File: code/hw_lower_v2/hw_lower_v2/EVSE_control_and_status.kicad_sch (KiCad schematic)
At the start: 13 parts, among them U3 DRV8220DRL, U4 TLV1805

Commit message: further lower board sch work
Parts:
- added C12, C13: 22uF 25V, Capacitor_SMD:C_1210_3225Metric, symbol Device:C
- C4: value C -> 100n; footprint (none) -> Capacitor_SMD:C_0805_2012Metric
- C5, C6: value C -> 100n 25V; footprint (none) -> Capacitor_SMD:C_0805_2012Metric
- R18, R19, R20, R21: footprint (none) -> Resistor_SMD:R_0603_1608Metric
- R22: value 1K -> 200k; footprint (none) -> Resistor_SMD:R_0603_1608Metric
- R23: value 1K -> 66.5k; footprint (none) -> Resistor_SMD:R_0603_1608Metric
- R24: value 1K -> 56k; footprint (none) -> Resistor_SMD:R_0603_1608Metric
- U3: footprint (none) -> Package_TO_SOT_SMD:SOT-563
- U4: footprint (none) -> Package_TO_SOT_SMD:SOT-23
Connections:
- net +12V: now also C12.1, C13.1
- net GND: now also C12.2, C13.2
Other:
- moved on the sheet: C4, C5, D2, R19, R20, R21, R22, R23, R24, U4

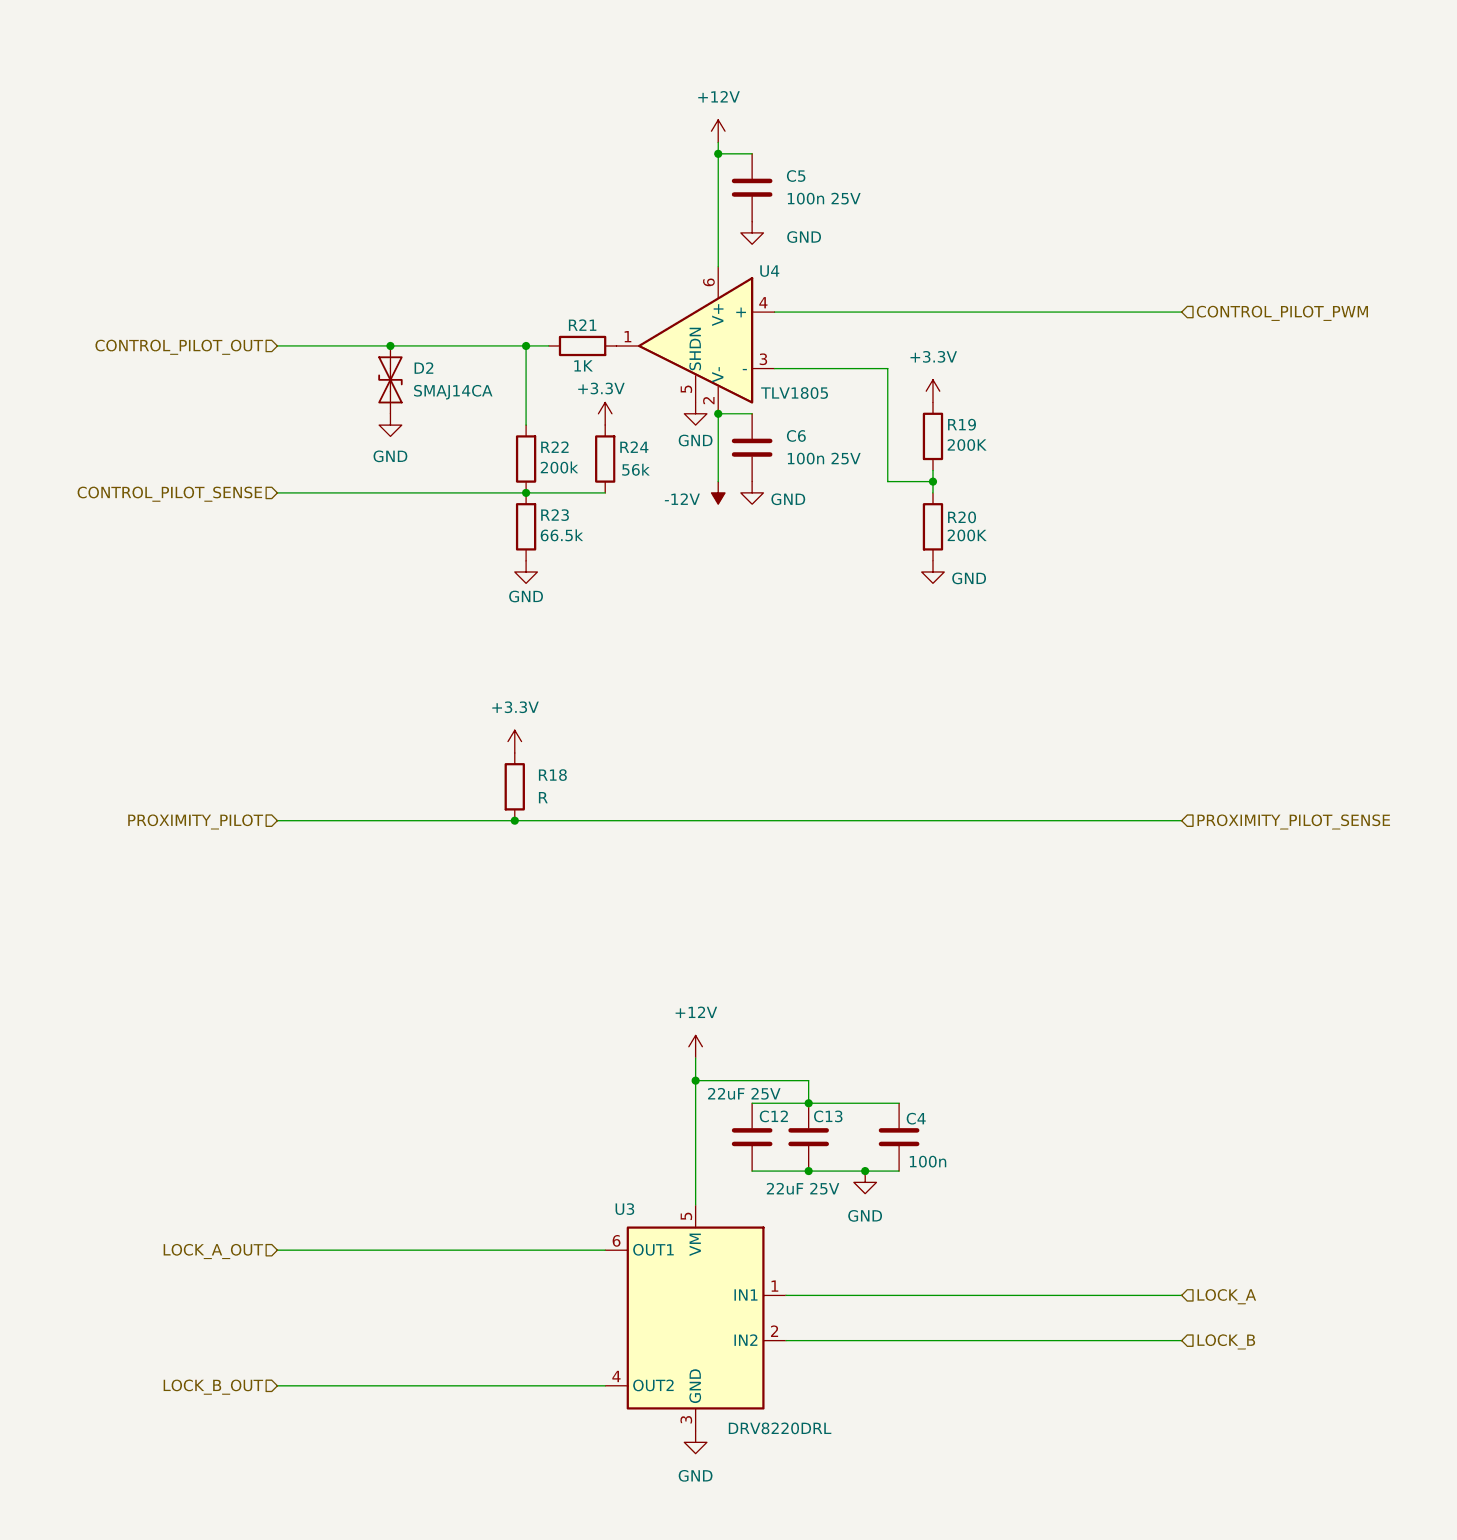
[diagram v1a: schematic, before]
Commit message: add 12V voltage inverter and polish
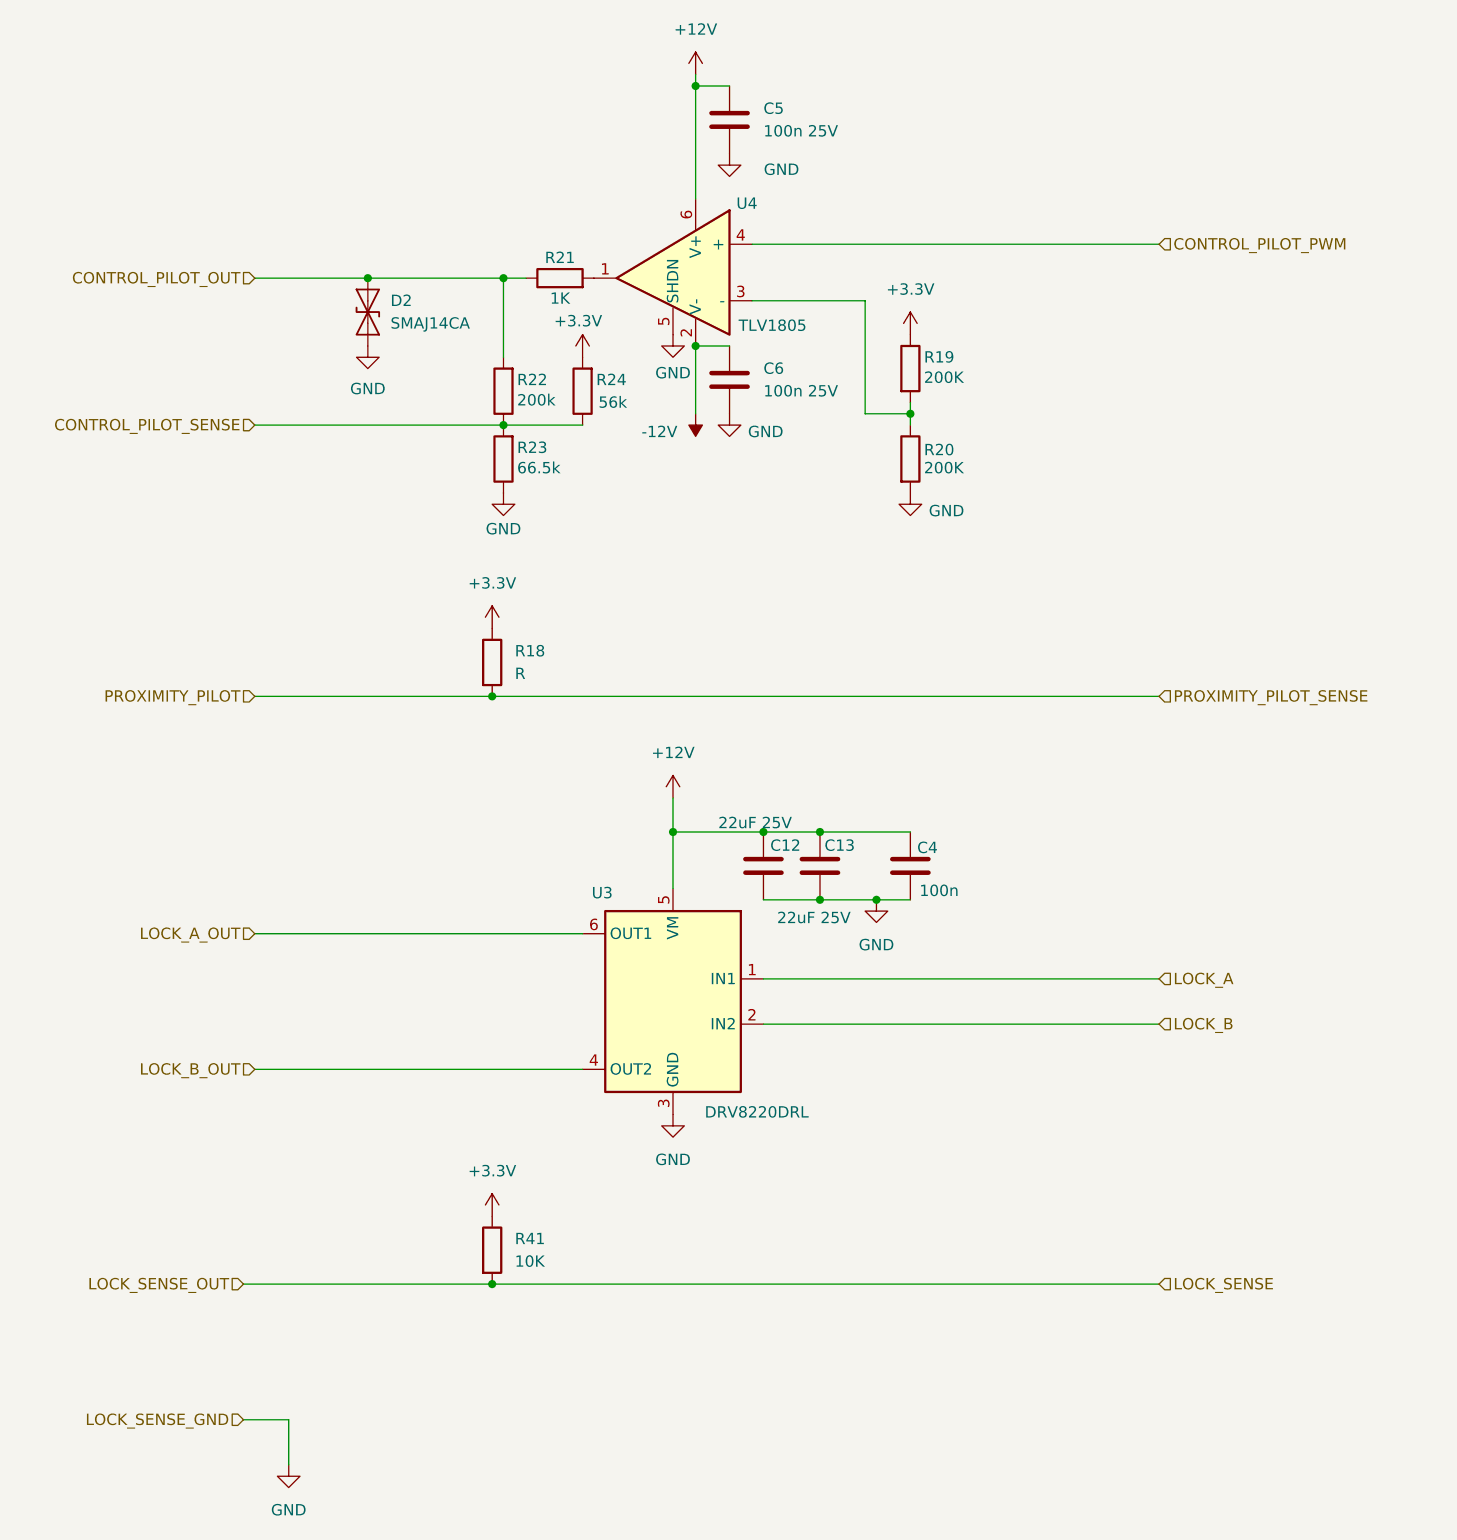
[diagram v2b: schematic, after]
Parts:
- added R41: 10K, Resistor_SMD:R_0603_1608Metric, symbol Device:R
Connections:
- net +3.3V: now also R41.1
- new net LOCK_SENSE: R41.2
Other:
- moved on the sheet: C12, C13, C4, C5, C6, D2, R18, R19, R20, R21, R22, R23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

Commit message: schematic is done
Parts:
- removed C12, C13: 22uF 25V, Capacitor_SMD:C_1210_3225Metric, symbol Device:C
- added C23: 10u, symbol Device:C_Polarized
- added D6: SMAJ5.0A, Diode_SMD:D_SMA, symbol Diode:SMAJ5.0A
- C5, C6: value 100n 25V -> 100n
- D2: JLCPCB Part # (none) -> C908820
- R18: value R -> 1K
- R22: value 200k -> 200k 1%
- R23: value 66.5k -> 66.5k 1%
- U3: JLCPCB Part # (none) -> C3681351
- U4: JLCPCB Part # (none) -> C2862164
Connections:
- net +12V: now also C23.1
- net GND: now also C23.2, D6.2 (A2)
- net LOCK_SENSE: now also D6.1 (A1)
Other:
- note added: "PP resistance 100ohm 10 mm2 62A 220ohm 6 mm2 32A 680ohm 2.5mm2 20A 1500ohm 1.5mm2 10A"
- moved on the sheet: C4, R24

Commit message: finishing up sch and creating footprints
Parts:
- renumbered C23 to C10, C4 to C11, C5 to C8, C6 to C9, D6 to D2, D2 to D3, R18 to R29, R41 to R30, R22 to R31, R23 to R32, R21 to R33, R24 to R34, R19 to R35, R20 to R36
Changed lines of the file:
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@@
 		(on_board yes)
 		(dnp no)
-		(property "Reference" "#PWR024"
+		(property "Reference" "#PWR047"
 			(at 101.6 35.56 0)
 			(effects
@@
 			(project "hw_lower_v2"
 				(path "/c5175f1c-553a-46da-abbd-483c59ad8dfa/8ba574d6-efbf-49a1-9fad-b0d96c57b1a3"
-					(reference "#PWR024")
+					(reference "#PWR047")
 					(unit 1)
 				)
@@
 		(on_board yes)
 		(dnp no)
-		(property "Reference" "#PWR028"
+		(property "Reference" "#PWR051"
 			(at 121.92 73.66 0)
 			(effects
@@
 			(project "hw_lower_v2"
 				(path "/c5175f1c-553a-46da-abbd-483c59ad8dfa/8ba574d6-efbf-49a1-9fad-b0d96c57b1a3"
-					(reference "#PWR028")
+					(reference "#PWR051")
 					(unit 1)
 				)
@@
 		(dnp no)
 		(fields_autoplaced yes)
-		(property "Reference" "#PWR020"
+		(property "Reference" "#PWR043"
 			(at 95.25 105.41 0)
 			(effects
@@
 			(project ""
 				(path "/c5175f1c-553a-46da-abbd-483c59ad8dfa/8ba574d6-efbf-49a1-9fad-b0d96c57b1a3"
-					(reference "#PWR020")
+					(reference "#PWR043")
 					(unit 1)
 				)
@@
 		(dnp no)
 		(fields_autoplaced yes)
-		(property "Reference" "R41"
+		(property "Reference" "R30"
 			(at 77.47 151.1299 0)
 			(effects
@@
 			(project "hw_lower_v2"
 				(path "/c5175f1c-553a-46da-abbd-483c59ad8dfa/8ba574d6-efbf-49a1-9fad-b0d96c57b1a3"
-					(reference "R41")
+					(reference "R30")
 					(unit 1)
 				)
@@
 		(dnp no)
 		(fields_autoplaced yes)
-		(property "Reference" "#PWR050"
+		(property "Reference" "#PWR049"
 			(at 110.49 119.38 0)
 			(effects
@@
 			(project "hw_lower_v2"
 				(path "/c5175f1c-553a-46da-abbd-483c59ad8dfa/8ba574d6-efbf-49a1-9fad-b0d96c57b1a3"
-					(reference "#PWR050")
+					(reference "#PWR049")
 					(unit 1)
 				)
@@
 		(on_board yes)
 		(dnp no)
-		(property "Reference" "R24"
+		(property "Reference" "R34"
 			(at 89.154 54.61 0)
 			(effects
@@
 			(project "hw_lower_v2"
 				(path "/c5175f1c-553a-46da-abbd-483c59ad8dfa/8ba574d6-efbf-49a1-9fad-b0d96c57b1a3"
-					(reference "R24")
+					(reference "R34")
 					(unit 1)
 				)
@@
 		(on_board yes)
 		(dnp no)
-		(property "Reference" "#PWR026"
+		(property "Reference" "#PWR046"
 			(at 97.79 54.61 0)
 			(effects
@@
 			(project ""
 				(path "/c5175f1c-553a-46da-abbd-483c59ad8dfa/8ba574d6-efbf-49a1-9fad-b0d96c57b1a3"
-					(reference "#PWR026")
+					(reference "#PWR046")
 					(unit 1)
 				)
@@
 		(on_board yes)
 		(dnp no)
-		(property "Reference" "R21"
+		(property "Reference" "R33"
 			(at 82.55 40.894 90)
 			(effects
@@
 			(project "hw_lower_v2"
 				(path "/c5175f1c-553a-46da-abbd-483c59ad8dfa/8ba574d6-efbf-49a1-9fad-b0d96c57b1a3"
-					(reference "R21")
+					(reference "R33")
 					(unit 1)
 				)
@@
 		(dnp no)
 		(fields_autoplaced yes)
-		(property "Reference" "D2"
+		(property "Reference" "D3"
 			(at 63.5 45.7199 90)
 			(effects
@@
 			(project ""
 				(path "/c5175f1c-553a-46da-abbd-483c59ad8dfa/8ba574d6-efbf-49a1-9fad-b0d96c57b1a3"
-					(reference "D2")
+					(reference "D3")
 					(unit 1)
 				)
@@
 		(dnp no)
 		(fields_autoplaced yes)
-		(property "Reference" "#PWR027"
+		(property "Reference" "#PWR050"
 			(at 121.92 53.34 0)
 			(effects
@@
 			(project "hw_lower_v2"
 				(path "/c5175f1c-553a-46da-abbd-483c59ad8dfa/8ba574d6-efbf-49a1-9fad-b0d96c57b1a3"
-					(reference "#PWR027")
+					(reference "#PWR050")
 					(unit 1)
 				)
@@
 		(on_board yes)
 		(dnp no)
-		(property "Reference" "#PWR034"
+		(property "Reference" "#PWR042"
 			(at 95.25 55.88 0)
 			(effects
@@
 			(project "hw_lower_v2"
 				(path "/c5175f1c-553a-46da-abbd-483c59ad8dfa/8ba574d6-efbf-49a1-9fad-b0d96c57b1a3"
-					(reference "#PWR034")
+					(reference "#PWR042")
 					(unit 1)
 				)
@@
 		(on_board yes)
 		(dnp no)
-		(property "Reference" "#PWR029"
+		(property "Reference" "#PWR040"
 			(at 76.2 73.66 0)
 			(effects
@@
 			(project "hw_lower_v2"
 				(path "/c5175f1c-553a-46da-abbd-483c59ad8dfa/8ba574d6-efbf-49a1-9fad-b0d96c57b1a3"
-					(reference "#PWR029")
+					(reference "#PWR040")
 					(unit 1)
 				)
@@
 		(on_board yes)
 		(dnp no)
-		(property "Reference" "#PWR023"
+		(property "Reference" "#PWR048"
 			(at 101.6 64.77 0)
 			(effects
@@
 			(project "hw_lower_v2"
 				(path "/c5175f1c-553a-46da-abbd-483c59ad8dfa/8ba574d6-efbf-49a1-9fad-b0d96c57b1a3"
-					(reference "#PWR023")
+					(reference "#PWR048")
 					(unit 1)
 				)
@@
 		(on_board yes)
 		(dnp no)
-		(property "Reference" "C23"
+		(property "Reference" "C10"
 			(at 105.664 106.68 0)
 			(effects
@@
 			(project "hw_lower_v2"
 				(path "/c5175f1c-553a-46da-abbd-483c59ad8dfa/8ba574d6-efbf-49a1-9fad-b0d96c57b1a3"
-					(reference "C23")
+					(reference "C10")
 					(unit 1)
 				)
@@
 		(dnp no)
 		(fields_autoplaced yes)
-		(property "Reference" "#PWR057"
+		(property "Reference" "#PWR039"
 			(at 74.93 152.4 0)
 			(effects
@@
 			(project "hw_lower_v2"
 				(path "/c5175f1c-553a-46da-abbd-483c59ad8dfa/8ba574d6-efbf-49a1-9fad-b0d96c57b1a3"
-					(reference "#PWR057")
+					(reference "#PWR039")
 					(unit 1)
 				)
@@
 		(dnp no)
 		(fields_autoplaced yes)
-		(property "Reference" "#PWR025"
+		(property "Reference" "#PWR045"
 			(at 97.79 24.13 0)
 			(effects
@@
 			(project ""
 				(path "/c5175f1c-553a-46da-abbd-483c59ad8dfa/8ba574d6-efbf-49a1-9fad-b0d96c57b1a3"
-					(reference "#PWR025")
+					(reference "#PWR045")
 					(unit 1)
 				)
@@
 		(dnp no)
 		(fields_autoplaced yes)
-		(property "Reference" "#PWR021"
+		(property "Reference" "#PWR044"
 			(at 95.25 143.51 0)
 			(effects
@@
 			(project ""
 				(path "/c5175f1c-553a-46da-abbd-483c59ad8dfa/8ba574d6-efbf-49a1-9fad-b0d96c57b1a3"
-					(reference "#PWR021")
+					(reference "#PWR044")
 					(unit 1)
 				)
@@
 		(dnp no)
 		(fields_autoplaced yes)
-		(property "Reference" "D6"
+		(property "Reference" "D2"
 			(at 53.34 162.5599 90)
 			(effects
@@
 			(project ""
 				(path "/c5175f1c-553a-46da-abbd-483c59ad8dfa/8ba574d6-efbf-49a1-9fad-b0d96c57b1a3"
-					(reference "D6")
+					(reference "D2")
 					(unit 1)
 				)
@@
 		(on_board yes)
 		(dnp no)
-		(property "Reference" "R19"
+		(property "Reference" "R35"
 			(at 123.444 52.07 0)
 			(effects
@@
 			(project "hw_lower_v2"
 				(path "/c5175f1c-553a-46da-abbd-483c59ad8dfa/8ba574d6-efbf-49a1-9fad-b0d96c57b1a3"
-					(reference "R19")
+					(reference "R35")
 					(unit 1)
 				)
@@
 		(on_board yes)
 		(dnp no)
-		(property "Reference" "R23"
+		(property "Reference" "R32"
 			(at 77.724 62.23 0)
 			(effects
@@
 			(project "hw_lower_v2"
 				(path "/c5175f1c-553a-46da-abbd-483c59ad8dfa/8ba574d6-efbf-49a1-9fad-b0d96c57b1a3"
-					(reference "R23")
+					(reference "R32")
 					(unit 1)
 				)
@@
 		(dnp no)
 		(fields_autoplaced yes)
-		(property "Reference" "#PWR019"
+		(property "Reference" "#PWR038"
 			(at 74.93 86.36 0)
 			(effects
@@
 			(project ""
 				(path "/c5175f1c-553a-46da-abbd-483c59ad8dfa/8ba574d6-efbf-49a1-9fad-b0d96c57b1a3"
-					(reference "#PWR019")
+					(reference "#PWR038")
 					(unit 1)
 				)
@@
 		(on_board yes)
 		(dnp no)
-		(property "Reference" "R20"
+		(property "Reference" "R36"
 			(at 123.444 62.484 0)
 			(effects
@@
 			(project "hw_lower_v2"
 				(path "/c5175f1c-553a-46da-abbd-483c59ad8dfa/8ba574d6-efbf-49a1-9fad-b0d96c57b1a3"
-					(reference "R20")
+					(reference "R36")
 					(unit 1)
 				)
@@
 		(on_board yes)
 		(dnp no)
-		(property "Reference" "#PWR030"
+		(property "Reference" "#PWR041"
 			(at 87.63 55.88 0)
 			(effects
@@
 			(project "hw_lower_v2"
 				(path "/c5175f1c-553a-46da-abbd-483c59ad8dfa/8ba574d6-efbf-49a1-9fad-b0d96c57b1a3"
-					(reference "#PWR030")
+					(reference "#PWR041")
 					(unit 1)
 				)
@@
 		(on_board yes)
 		(dnp no)
-		(property "Reference" "#PWR031"
+		(property "Reference" "#PWR037"
 			(at 60.96 57.15 0)
 			(effects
@@
 			(project "hw_lower_v2"
 				(path "/c5175f1c-553a-46da-abbd-483c59ad8dfa/8ba574d6-efbf-49a1-9fad-b0d96c57b1a3"
-					(reference "#PWR031")
+					(reference "#PWR037")
 					(unit 1)
 				)
@@
 		(dnp no)
 		(fields_autoplaced yes)
-		(property "Reference" "C6"
+		(property "Reference" "C9"
 			(at 105.41 53.3399 0)
 			(effects
@@
 			(project "hw_lower_v2"
 				(path "/c5175f1c-553a-46da-abbd-483c59ad8dfa/8ba574d6-efbf-49a1-9fad-b0d96c57b1a3"
-					(reference "C6")
+					(reference "C9")
 					(unit 1)
 				)
@@
 		(dnp no)
 		(fields_autoplaced yes)
-		(property "Reference" "C5"
+		(property "Reference" "C8"
 			(at 105.41 24.1299 0)
 			(effects
@@
 			(project "hw_lower_v2"
 				(path "/c5175f1c-553a-46da-abbd-483c59ad8dfa/8ba574d6-efbf-49a1-9fad-b0d96c57b1a3"
-					(reference "C5")
+					(reference "C8")
 					(unit 1)
 				)
@@
 		(dnp no)
 		(fields_autoplaced yes)
-		(property "Reference" "R18"
+		(property "Reference" "R29"
 			(at 77.47 85.0899 0)
 			(effects
@@
 			(project ""
 				(path "/c5175f1c-553a-46da-abbd-483c59ad8dfa/8ba574d6-efbf-49a1-9fad-b0d96c57b1a3"
-					(reference "R18")
+					(reference "R29")
 					(unit 1)
 				)
@@
 		(on_board yes)
 		(dnp no)
-		(property "Reference" "R22"
+		(property "Reference" "R31"
 			(at 77.724 54.61 0)
 			(effects
@@
 			(project "hw_lower_v2"
 				(path "/c5175f1c-553a-46da-abbd-483c59ad8dfa/8ba574d6-efbf-49a1-9fad-b0d96c57b1a3"
-					(reference "R22")
+					(reference "R31")
 					(unit 1)
 				)
@@
 		(on_board yes)
 		(dnp no)
-		(property "Reference" "C4"
+		(property "Reference" "C11"
 			(at 115.062 107.188 0)
 			(effects
@@
 			(project ""
 				(path "/c5175f1c-553a-46da-abbd-483c59ad8dfa/8ba574d6-efbf-49a1-9fad-b0d96c57b1a3"
-					(reference "C4")
+					(reference "C11")
 					(unit 1)
 				)
@@
 		(dnp no)
 		(fields_autoplaced yes)
-		(property "Reference" "#PWR055"
+		(property "Reference" "#PWR036"
 			(at 50.8 182.88 0)
 			(effects
@@
 			(project "hw_lower_v2"
 				(path "/c5175f1c-553a-46da-abbd-483c59ad8dfa/8ba574d6-efbf-49a1-9fad-b0d96c57b1a3"
-					(reference "#PWR055")
-					(unit 1)
-				)
+					(reference "#PWR036")
+					(unit 1)
+				)
